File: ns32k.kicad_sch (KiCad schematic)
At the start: 50 parts, among them SW2 SW_DIP_x04, U1 NS32201, U10 74AHC373, U11 74AHC373, U12 74AHC138, U13 AS6C6416-55, U15 MX29LV040C, U16 MX29LV040C, U19 74AHC32, U20 74AHC1GU04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

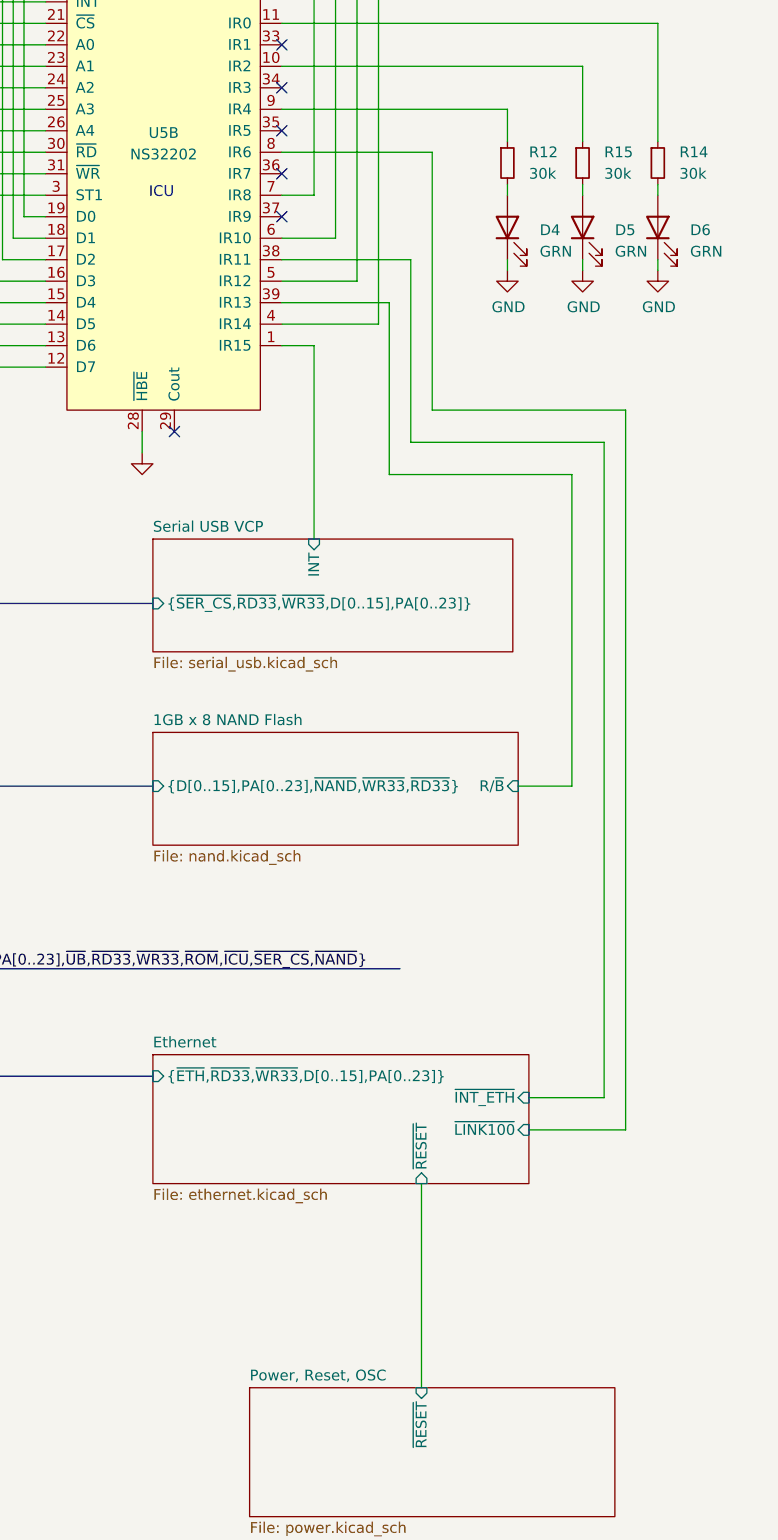
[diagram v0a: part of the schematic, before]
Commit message: Rework RESET/RST: see Changelist
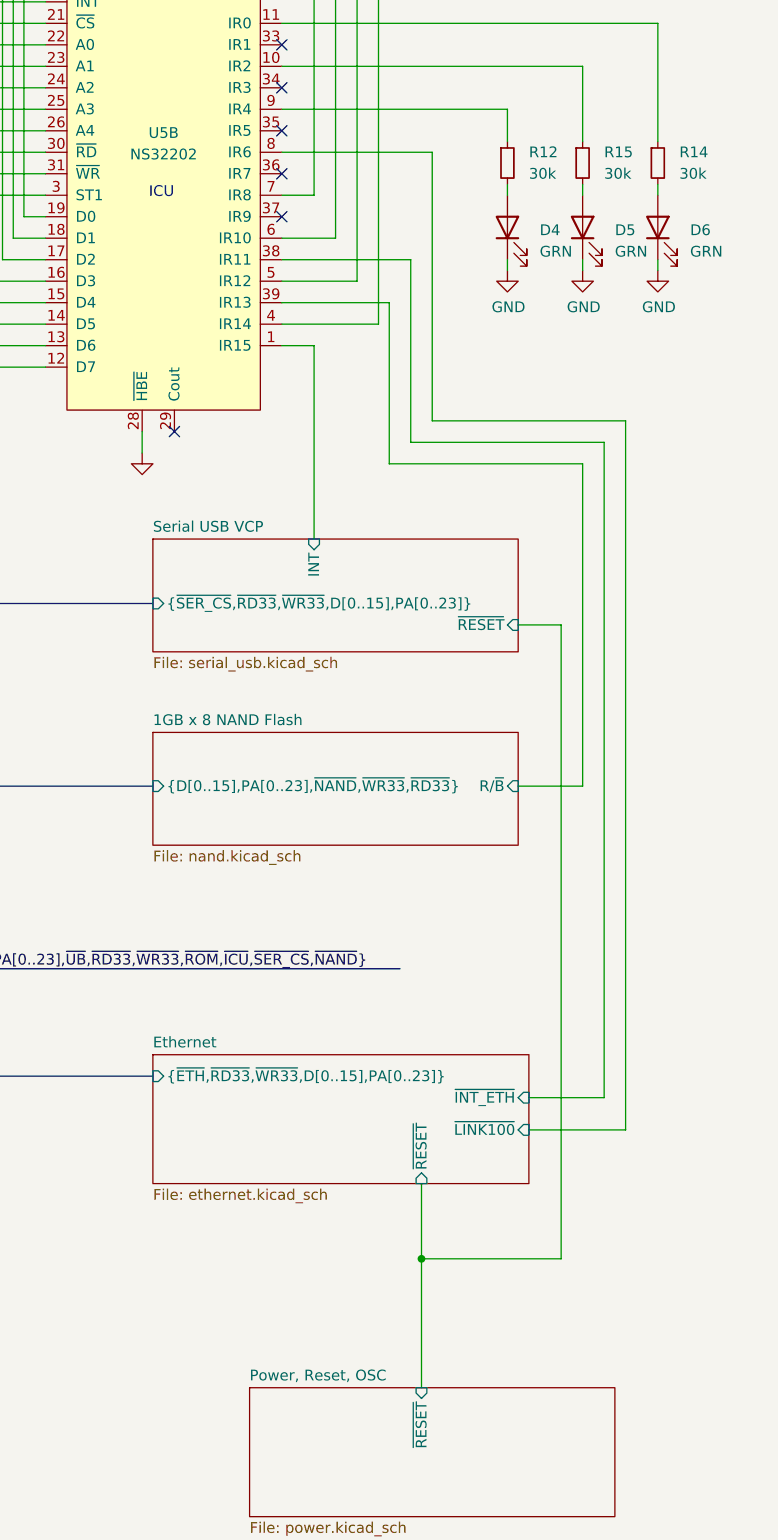
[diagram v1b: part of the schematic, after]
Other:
- sheet Serial USB VCP ports: added ~{RESET}; removed none
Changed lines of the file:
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@@
 	)
 	(junction
+		(at 359.41 203.2)
+		(diameter 0)
+		(color 0 0 0 0)
+	)
+	(junction
 		(at 278.13 114.3)
 		(diameter 0)
@@
 	(wire
 		(pts
-			(xy 359.41 194.31) (xy 359.41 218.44)
+			(xy 359.41 194.31) (xy 359.41 203.2)
 		)
 		(stroke
@@
 		)
 	)
+	(wire
+		(pts
+			(xy 375.92 203.2) (xy 359.41 203.2)
+		)
+		(stroke
+			(width 0)
+			(type default)
+		)
+	)
 	(bus
 		(pts
@@
 	(wire
 		(pts
-			(xy 377.19 110.49) (xy 355.6 110.49)
+			(xy 378.46 109.22) (xy 355.6 109.22)
 		)
 		(stroke
@@
 	(wire
 		(pts
+			(xy 370.84 128.27) (xy 375.92 128.27)
+		)
+		(stroke
+			(width 0)
+			(type default)
+		)
+	)
+	(wire
+		(pts
 			(xy 219.71 158.75) (xy 219.71 161.29)
 		)
@@
 	(wire
 		(pts
-			(xy 370.84 147.32) (xy 377.19 147.32)
+			(xy 370.84 147.32) (xy 378.46 147.32)
 		)
 		(stroke
@@
 	(wire
 		(pts
+			(xy 375.92 128.27) (xy 375.92 203.2)
+		)
+		(stroke
+			(width 0)
+			(type default)
+		)
+	)
+	(wire
+		(pts
 			(xy 274.32 46.99) (xy 303.53 46.99)
 		)
@@
 	(wire
 		(pts
+			(xy 359.41 203.2) (xy 359.41 218.44)
+		)
+		(stroke
+			(width 0)
+			(type default)
+		)
+	)
+	(wire
+		(pts
 			(xy 306.07 41.91) (xy 306.07 92.71)
 		)
@@
 	(wire
 		(pts
-			(xy 360.68 72.39) (xy 360.68 102.87)
+			(xy 360.68 72.39) (xy 360.68 104.14)
 		)
 		(stroke
@@
 	(wire
 		(pts
-			(xy 383.54 102.87) (xy 383.54 187.96)
+			(xy 383.54 104.14) (xy 383.54 187.96)
 		)
 		(stroke
@@
 	(wire
 		(pts
-			(xy 377.19 147.32) (xy 377.19 110.49)
+			(xy 378.46 147.32) (xy 378.46 109.22)
 		)
 		(stroke
@@
 	(wire
 		(pts
-			(xy 360.68 102.87) (xy 383.54 102.87)
+			(xy 360.68 104.14) (xy 383.54 104.14)
 		)
 		(stroke
@@
 	(wire
 		(pts
-			(xy 355.6 110.49) (xy 355.6 90.17)
+			(xy 355.6 109.22) (xy 355.6 90.17)
 		)
 		(stroke
@@
 	(sheet
 		(at 327.66 118.11)
-		(size 42.545 13.335)
+		(size 43.18 13.335)
 		(fields_autoplaced yes)
 		(stroke
@@
 			)
 		)
+		(pin "~{RESET}" input
+			(at 370.84 128.27 0)
+			(effects
+				(font
+					(size 1.27 1.27)
+				)
+				(justify right)
+			)
+		)

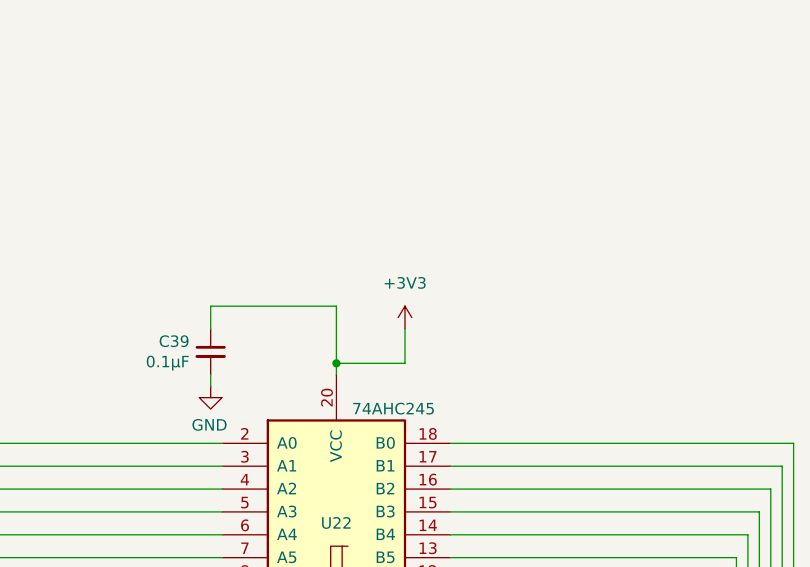
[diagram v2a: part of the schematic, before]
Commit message: Power ICU AHC245 buffer with +5V
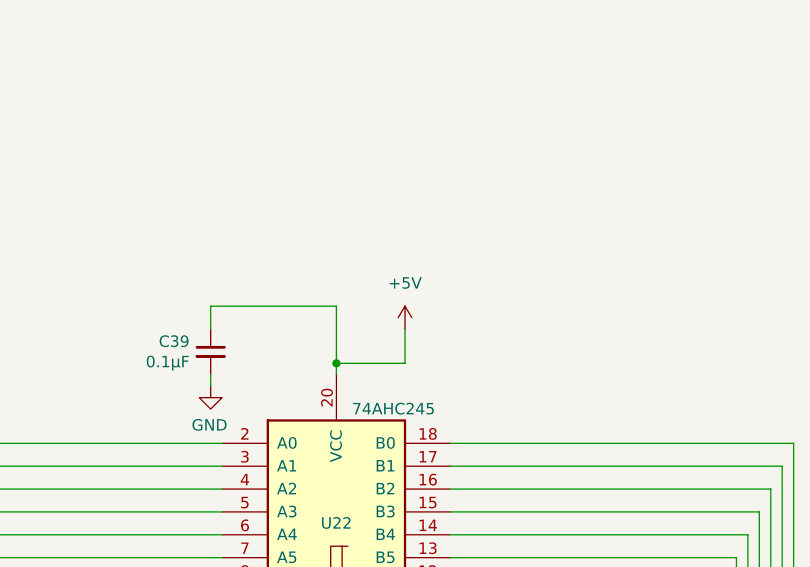
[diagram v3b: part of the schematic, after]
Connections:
- net +3V3: no longer C39.1, U22.20 (VCC)
- net +5V: now also C39.1, U22.20 (VCC)
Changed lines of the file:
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@@
 	)
 	(symbol
+		(lib_id "power:+5V")
+		(at 269.24 16.51 0)
+		(unit 1)
+		(exclude_from_sim no)
+		(in_bom yes)
+		(on_board yes)
+		(dnp no)
+		(fields_autoplaced yes)
+		(property "Reference" "#PWR0114"
+			(at 269.24 20.32 0)
+			(effects
+				(font
+					(size 1.27 1.27)
+				)
+				(hide yes)
+			)
+		)
+		(property "Value" "+5V"
+			(at 269.24 11.43 0)
+			(effects
+				(font
+					(size 1.27 1.27)
+				)
+			)
+		)
+		(property "Footprint" ""
+			(at 269.24 16.51 0)
+			(effects
+				(font
+					(size 1.27 1.27)
+				)
+				(hide yes)
+			)
+		)
+		(property "Datasheet" ""
+			(at 269.24 16.51 0)
+			(effects
+				(font
+					(size 1.27 1.27)
+				)
+				(hide yes)
+			)
+		)
+		(property "Description" "Power symbol creates a global label with name \"+5V\""
+			(at 269.24 16.51 0)
+			(effects
+				(font
+					(size 1.27 1.27)
+				)
+				(hide yes)
+			)
+		)
+		(pin "1"
+		)
+		(instances
+			(project ""
+				(path "/54787df0-1b8c-465f-acae-f55ec7f02da3"
+					(reference "#PWR0114")
+					(unit 1)
+				)
+			)
+		)
+	)
+	(symbol
 		(lib_id "Device:R_Small")
 		(at 378.46 73.66 0)
@@
 					(unit 1)
 				)
-			)
-		)
-	)
-	(symbol
-		(lib_id "power:+3V3")
-		(at 269.24 16.51 0)
-		(unit 1)
-		(exclude_from_sim no)
-		(in_bom yes)
-		(on_board yes)
-		(dnp no)
-		(fields_autoplaced yes)
-		(property "Reference" "#PWR0114"
-			(at 269.24 20.32 0)
-			(effects
-				(font
-					(size 1.27 1.27)
-				)
-				(hide yes)
-			)
-		)
-		(property "Value" "+3V3"
-			(at 269.24 11.43 0)
-			(effects
-				(font
-					(size 1.27 1.27)
-				)
-			)
-		)
-		(property "Footprint" ""
-			(at 269.24 16.51 0)
-			(effects
-				(font
-					(size 1.27 1.27)
-				)
-				(hide yes)
-			)
-		)
-		(property "Datasheet" ""
-			(at 269.24 16.51 0)
-			(effects
-				(font
-					(size 1.27 1.27)
-				)
-				(hide yes)
-			)
-		)
-		(property "Description" "Power symbol creates a global label with name \"+3V3\""
-			(at 269.24 16.51 0)
-			(effects
-				(font
-					(size 1.27 1.27)
-				)
-				(hide yes)
-			)
-		)
-		(pin "1"
-		)
-		(instances
-			(project ""
-				(path "/54787df0-1b8c-465f-acae-f55ec7f02da3"
-					(reference "#PWR0114")
-					(unit 1)
-				)

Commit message: fix address decoding
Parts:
- removed C23, C24, C25, C26, C56: 50pF, Capacitor_SMD:C_0402_1005Metric, symbol Device:C_Small
- added U24: 74AHC1GU04, Package_TO_SOT_SMD:SOT-23-5, symbol 74xGxx:74AHC1GU04
- added unit 4 of U6
- C13, C17, C19, C21, C22, C27, C29, C32, C33, C39, C58: LCSC (none) -> C466613
- D4, D5, D6: LCSC (none) -> C5246833
- R11, R2, R3, R4, R5, R7: LCSC (none) -> C375970
- R12, R14, R15, R26, R27, R28, R29: LCSC (none) -> C2906928
- SW2: LCSC (none) -> C18198092
- U10, U11, U9: LCSC (none) -> C80242
- U12: LCSC (none) -> C352950
- U13: LCSC (none) -> C1349200
- U19: LCSC (none) -> C2868909
- U20: LCSC (none) -> C352954
- U22, U7, U8: LCSC (none) -> C5516
- U6: LCSC (none) -> C2863502
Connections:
- net +3V3: now also U24.5 (VCC)
- net GND: now also U24.3 (GND); no longer U12.4 (E1), U13.26 (~{CE})
- net ~{ADS}: now also U1.6 (~{ADS})
- net ~{DBE}: now also U6.12
- net ~{PAV}: now also U24.2; no longer U1.6 (~{ADS}), U10.11 (LE), U11.11 (LE), U9.11 (LE)
- net ~{TSO}: now reaches U1.17 (~{TSO})
- net ~{TSO}: now also U6.13
- new net PAV: U10.11 (LE), U11.11 (LE), U24.4, U9.11 (LE)
- new net ~{CS_E}: U12.4 (E1), U13.26 (~{CE}), U6.11
- no-connect marks 12 -> 11
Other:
- note added: "~{CS_E} is a general CS# enable."

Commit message: add rev4 gerbers, bom files
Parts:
- SW2: value SW_DIP_x04 -> SW_DIP_x04 300w/50p mil
- U15, U16: value MX29LV040C -> MX29LV040C DNP
- U3: value NS32016 -> NS32016 DNP
- U4: value NS32082 -> NS32082 DNP
- U5: value NS32202 -> NS32202 DNP
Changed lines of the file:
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@@
 			)
 		)
-		(property "Value" "NS32016"
+		(property "Value" "NS32016 DNP"
 			(at 59.69 109.22 0)
 			(effects
@@
 			)
 		)
-		(property "Value" "NS32082"
+		(property "Value" "NS32082 DNP"
 			(at 143.51 44.45 0)
 			(effects
@@
 			)
 		)
-		(property "Value" "SW_DIP_x04"
+		(property "Value" "SW_DIP_x04 300w/50p mil"
 			(at 388.62 29.21 0)
 			(effects
@@
 			)
 		)
-		(property "Value" "MX29LV040C"
+		(property "Value" "MX29LV040C DNP"
 			(at 253.492 213.868 0)
 			(effects
@@
 			)
 		)
-		(property "Value" "MX29LV040C"
+		(property "Value" "MX29LV040C DNP"
 			(at 166.878 213.868 0)
 			(effects
@@
 			)
 		)
-		(property "Value" "NS32202"
+		(property "Value" "NS32202 DNP"
 			(at 328.93 72.644 0)
 			(effects
